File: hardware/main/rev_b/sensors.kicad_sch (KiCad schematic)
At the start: 16 parts, among them U20 ICM-42688-P, U21 LSM6DSO32TR, U22 LPS22DFTR

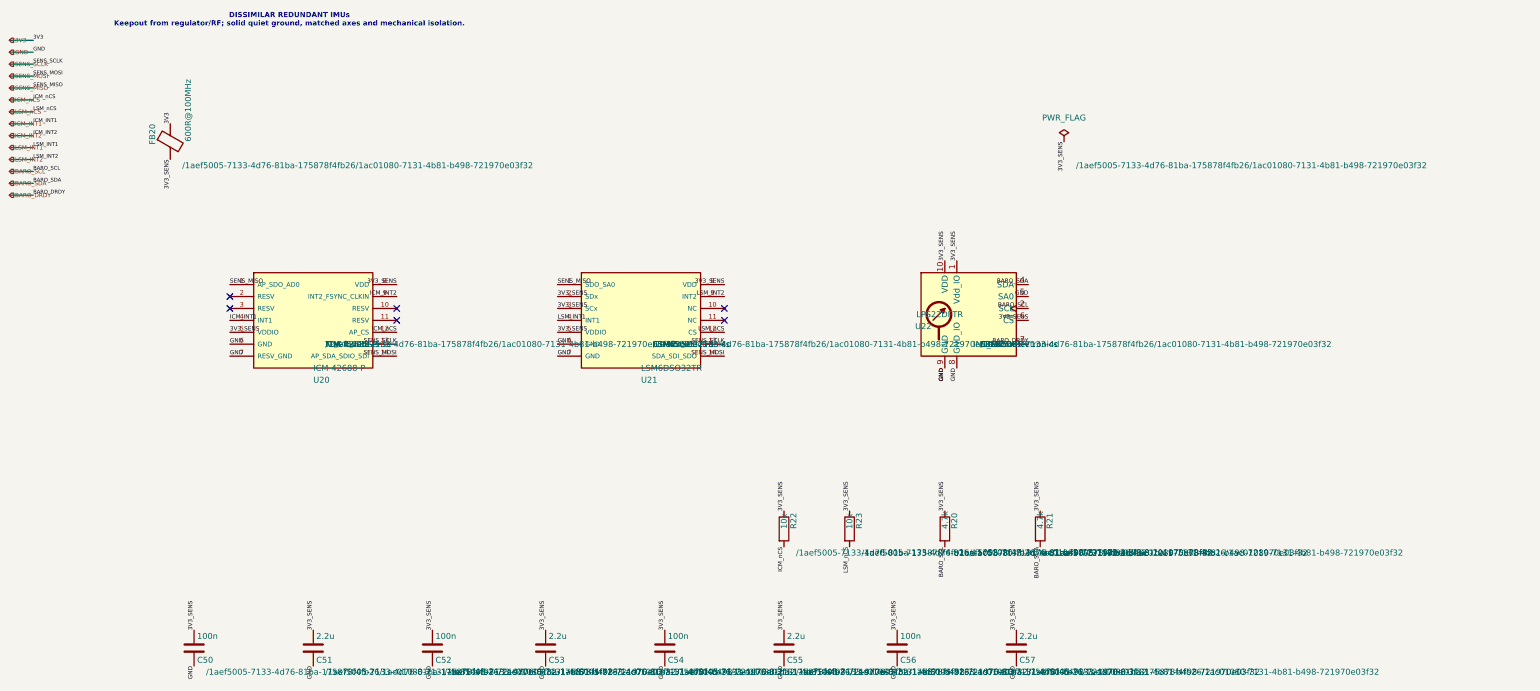
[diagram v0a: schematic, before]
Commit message: build: route and validate rev-b boards
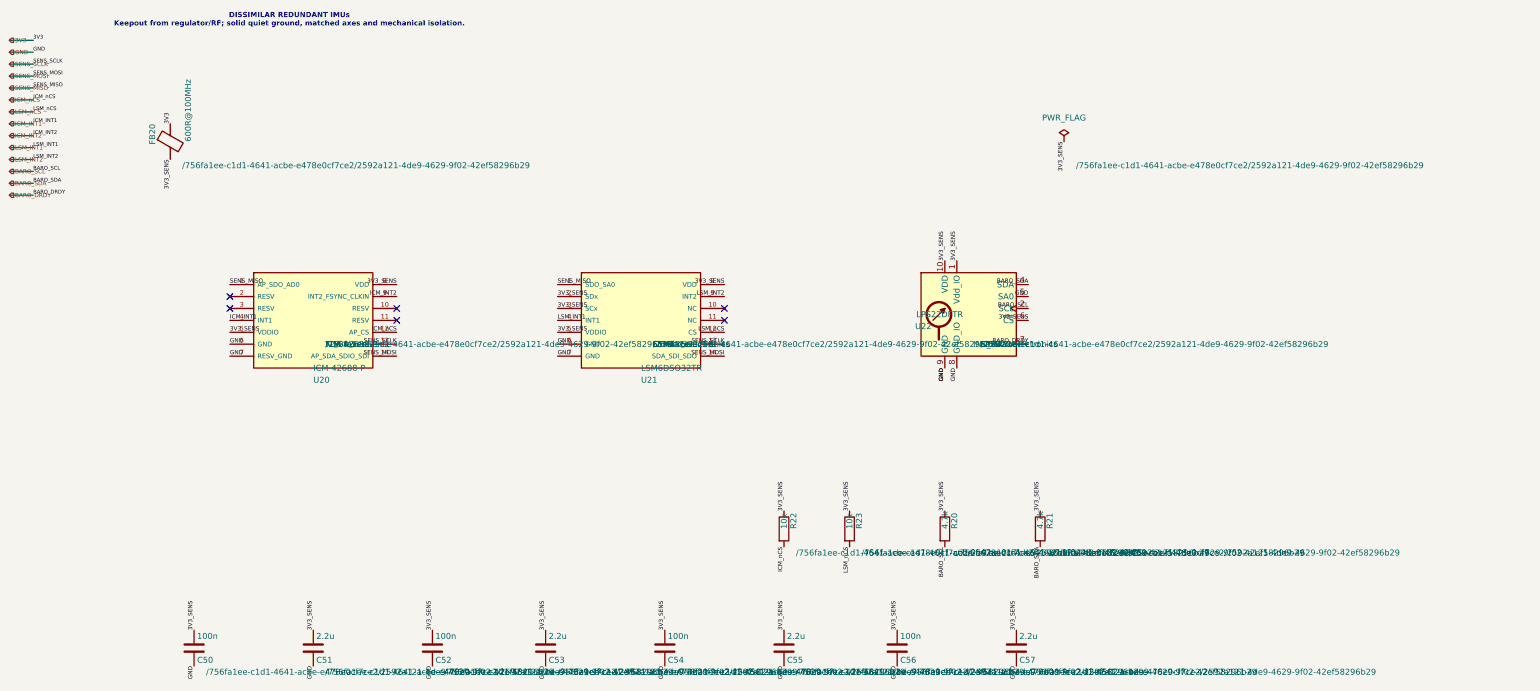
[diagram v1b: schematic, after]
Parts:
- C50, C51, C52, C53, C54, C55, C56, C57, FB20, R20, R21, R22, R23, U20, U21, U22: hierarchy_path /1aef5005-7133-4d76-81ba-175878f4fb26/1ac01080-7131-4b81-b4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 -> /756fa1ee-c1d1-4641-acbe-e478e0cf7ce2/2592a121-4de9-4629-9f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
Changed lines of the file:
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@@
 			)
 		)
-		(property "hierarchy_path" "/1aef5005-7133-4d76-81ba-175878f4fb26/1ac01080-7131-4b81-b498-721970e03f32"
+		(property "hierarchy_path" "/756fa1ee-c1d1-4641-acbe-e478e0cf7ce2/2592a121-4de9-4629-9f02-42ef58296b29"
 			(at 57.15 46.9899 0)
 			(effects
@@
 		(instances
 			(project "main_rev_b"
-				(path "/1aef5005-7133-4d76-81ba-175878f4fb26/1ac01080-7131-4b81-b498-721970e03f32"
+				(path "/756fa1ee-c1d1-4641-acbe-e478e0cf7ce2/2592a121-4de9-4629-9f02-42ef58296b29"
 					(reference "FB20")
 					(unit 1)
@@
 			)
 		)
-		(property "hierarchy_path" "/1aef5005-7133-4d76-81ba-175878f4fb26/1ac01080-7131-4b81-b498-721970e03f32"
+		(property "hierarchy_path" "/756fa1ee-c1d1-4641-acbe-e478e0cf7ce2/2592a121-4de9-4629-9f02-42ef58296b29"
 			(at 87.63 85.0899 0)
 			(effects
@@
 		(instances
 			(project "main_rev_b"
-				(path "/1aef5005-7133-4d76-81ba-175878f4fb26/1ac01080-7131-4b81-b498-721970e03f32"
+				(path "/756fa1ee-c1d1-4641-acbe-e478e0cf7ce2/2592a121-4de9-4629-9f02-42ef58296b29"
 					(reference "U20")
 					(unit 1)
@@
 			)
 		)
-		(property "hierarchy_path" "/1aef5005-7133-4d76-81ba-175878f4fb26/1ac01080-7131-4b81-b498-721970e03f32"
+		(property "hierarchy_path" "/756fa1ee-c1d1-4641-acbe-e478e0cf7ce2/2592a121-4de9-4629-9f02-42ef58296b29"
 			(at 157.48 85.0899 0)
 			(effects
@@
 		(instances
 			(project "main_rev_b"
-				(path "/1aef5005-7133-4d76-81ba-175878f4fb26/1ac01080-7131-4b81-b498-721970e03f32"
+				(path "/756fa1ee-c1d1-4641-acbe-e478e0cf7ce2/2592a121-4de9-4629-9f02-42ef58296b29"
 					(reference "U21")
 					(unit 1)
@@
 			)
 		)
-		(property "hierarchy_path" "/1aef5005-7133-4d76-81ba-175878f4fb26/1ac01080-7131-4b81-b498-721970e03f32"
+		(property "hierarchy_path" "/756fa1ee-c1d1-4641-acbe-e478e0cf7ce2/2592a121-4de9-4629-9f02-42ef58296b29"
 			(at 227.33 85.0899 0)
 			(effects
@@
 		(instances
 			(project "main_rev_b"
-				(path "/1aef5005-7133-4d76-81ba-175878f4fb26/1ac01080-7131-4b81-b498-721970e03f32"
+				(path "/756fa1ee-c1d1-4641-acbe-e478e0cf7ce2/2592a121-4de9-4629-9f02-42ef58296b29"
 					(reference "U22")
 					(unit 1)
@@
 			)
 		)
-		(property "hierarchy_path" "/1aef5005-7133-4d76-81ba-175878f4fb26/1ac01080-7131-4b81-b498-721970e03f32"
+		(property "hierarchy_path" "/756fa1ee-c1d1-4641-acbe-e478e0cf7ce2/2592a121-4de9-4629-9f02-42ef58296b29"
 			(at 222.25 129.5399 0)
 			(effects
@@
 		(instances
 			(project "main_rev_b"
-				(path "/1aef5005-7133-4d76-81ba-175878f4fb26/1ac01080-7131-4b81-b498-721970e03f32"
+				(path "/756fa1ee-c1d1-4641-acbe-e478e0cf7ce2/2592a121-4de9-4629-9f02-42ef58296b29"
 					(reference "R20")
 					(unit 1)
@@
 			)
 		)
-		(property "hierarchy_path" "/1aef5005-7133-4d76-81ba-175878f4fb26/1ac01080-7131-4b81-b498-721970e03f32"
+		(property "hierarchy_path" "/756fa1ee-c1d1-4641-acbe-e478e0cf7ce2/2592a121-4de9-4629-9f02-42ef58296b29"
 			(at 242.57 129.5399 0)
 			(effects
@@
 		(instances
 			(project "main_rev_b"
-				(path "/1aef5005-7133-4d76-81ba-175878f4fb26/1ac01080-7131-4b81-b498-721970e03f32"
+				(path "/756fa1ee-c1d1-4641-acbe-e478e0cf7ce2/2592a121-4de9-4629-9f02-42ef58296b29"
 					(reference "R21")
 					(unit 1)
@@
 			)
 		)
-		(property "hierarchy_path" "/1aef5005-7133-4d76-81ba-175878f4fb26/1ac01080-7131-4b81-b498-721970e03f32"
+		(property "hierarchy_path" "/756fa1ee-c1d1-4641-acbe-e478e0cf7ce2/2592a121-4de9-4629-9f02-42ef58296b29"
 			(at 187.96 129.5399 0)
 			(effects
@@
 		(instances
 			(project "main_rev_b"
-				(path "/1aef5005-7133-4d76-81ba-175878f4fb26/1ac01080-7131-4b81-b498-721970e03f32"
+				(path "/756fa1ee-c1d1-4641-acbe-e478e0cf7ce2/2592a121-4de9-4629-9f02-42ef58296b29"
 					(reference "R22")
 					(unit 1)
@@
 			)
 		)
-		(property "hierarchy_path" "/1aef5005-7133-4d76-81ba-175878f4fb26/1ac01080-7131-4b81-b498-721970e03f32"
+		(property "hierarchy_path" "/756fa1ee-c1d1-4641-acbe-e478e0cf7ce2/2592a121-4de9-4629-9f02-42ef58296b29"
 			(at 201.93 129.5399 0)
 			(effects
@@
 		(instances
 			(project "main_rev_b"
-				(path "/1aef5005-7133-4d76-81ba-175878f4fb26/1ac01080-7131-4b81-b498-721970e03f32"
+				(path "/756fa1ee-c1d1-4641-acbe-e478e0cf7ce2/2592a121-4de9-4629-9f02-42ef58296b29"
 					(reference "R23")
 					(unit 1)
@@
 			)
 		)
-		(property "hierarchy_path" "/1aef5005-7133-4d76-81ba-175878f4fb26/1ac01080-7131-4b81-b498-721970e03f32"
+		(property "hierarchy_path" "/756fa1ee-c1d1-4641-acbe-e478e0cf7ce2/2592a121-4de9-4629-9f02-42ef58296b29"
 			(at 62.23 154.9399 0)
 			(effects
@@
 		(instances
 			(project "main_rev_b"
-				(path "/1aef5005-7133-4d76-81ba-175878f4fb26/1ac01080-7131-4b81-b498-721970e03f32"
+				(path "/756fa1ee-c1d1-4641-acbe-e478e0cf7ce2/2592a121-4de9-4629-9f02-42ef58296b29"
 					(reference "C50")
 					(unit 1)
@@
 			)
 		)
-		(property "hierarchy_path" "/1aef5005-7133-4d76-81ba-175878f4fb26/1ac01080-7131-4b81-b498-721970e03f32"
+		(property "hierarchy_path" "/756fa1ee-c1d1-4641-acbe-e478e0cf7ce2/2592a121-4de9-4629-9f02-42ef58296b29"
 			(at 87.63 154.9399 0)
 			(effects
@@
 		(instances
 			(project "main_rev_b"
-				(path "/1aef5005-7133-4d76-81ba-175878f4fb26/1ac01080-7131-4b81-b498-721970e03f32"
+				(path "/756fa1ee-c1d1-4641-acbe-e478e0cf7ce2/2592a121-4de9-4629-9f02-42ef58296b29"
 					(reference "C51")
 					(unit 1)
@@
 			)
 		)
-		(property "hierarchy_path" "/1aef5005-7133-4d76-81ba-175878f4fb26/1ac01080-7131-4b81-b498-721970e03f32"
+		(property "hierarchy_path" "/756fa1ee-c1d1-4641-acbe-e478e0cf7ce2/2592a121-4de9-4629-9f02-42ef58296b29"
 			(at 113.03 154.9399 0)
 			(effects
@@
 		(instances
 			(project "main_rev_b"
-				(path "/1aef5005-7133-4d76-81ba-175878f4fb26/1ac01080-7131-4b81-b498-721970e03f32"
+				(path "/756fa1ee-c1d1-4641-acbe-e478e0cf7ce2/2592a121-4de9-4629-9f02-42ef58296b29"
 					(reference "C52")
 					(unit 1)
@@
 			)
 		)
-		(property "hierarchy_path" "/1aef5005-7133-4d76-81ba-175878f4fb26/1ac01080-7131-4b81-b498-721970e03f32"
+		(property "hierarchy_path" "/756fa1ee-c1d1-4641-acbe-e478e0cf7ce2/2592a121-4de9-4629-9f02-42ef58296b29"
 			(at 137.16 154.9399 0)
 			(effects
@@
 		(instances
 			(project "main_rev_b"
-				(path "/1aef5005-7133-4d76-81ba-175878f4fb26/1ac01080-7131-4b81-b498-721970e03f32"
+				(path "/756fa1ee-c1d1-4641-acbe-e478e0cf7ce2/2592a121-4de9-4629-9f02-42ef58296b29"
 					(reference "C53")
 					(unit 1)
@@
 			)
 		)
-		(property "hierarchy_path" "/1aef5005-7133-4d76-81ba-175878f4fb26/1ac01080-7131-4b81-b498-721970e03f32"
+		(property "hierarchy_path" "/756fa1ee-c1d1-4641-acbe-e478e0cf7ce2/2592a121-4de9-4629-9f02-42ef58296b29"
 			(at 162.56 154.9399 0)
 			(effects
@@
 		(instances
 			(project "main_rev_b"
-				(path "/1aef5005-7133-4d76-81ba-175878f4fb26/1ac01080-7131-4b81-b498-721970e03f32"
+				(path "/756fa1ee-c1d1-4641-acbe-e478e0cf7ce2/2592a121-4de9-4629-9f02-42ef58296b29"
 					(reference "C54")
 					(unit 1)
@@
 			)
 		)
-		(property "hierarchy_path" "/1aef5005-7133-4d76-81ba-175878f4fb26/1ac01080-7131-4b81-b498-721970e03f32"
+		(property "hierarchy_path" "/756fa1ee-c1d1-4641-acbe-e478e0cf7ce2/2592a121-4de9-4629-9f02-42ef58296b29"
 			(at 187.96 154.9399 0)
 			(effects
@@
 		(instances
 			(project "main_rev_b"
-				(path "/1aef5005-7133-4d76-81ba-175878f4fb26/1ac01080-7131-4b81-b498-721970e03f32"
+				(path "/756fa1ee-c1d1-4641-acbe-e478e0cf7ce2/2592a121-4de9-4629-9f02-42ef58296b29"
 					(reference "C55")
 					(unit 1)
@@
 			)
 		)
-		(property "hierarchy_path" "/1aef5005-7133-4d76-81ba-175878f4fb26/1ac01080-7131-4b81-b498-721970e03f32"
+		(property "hierarchy_path" "/756fa1ee-c1d1-4641-acbe-e478e0cf7ce2/2592a121-4de9-4629-9f02-42ef58296b29"
 			(at 212.09 154.9399 0)
 			(effects
@@
 		(instances
 			(project "main_rev_b"
-				(path "/1aef5005-7133-4d76-81ba-175878f4fb26/1ac01080-7131-4b81-b498-721970e03f32"
+				(path "/756fa1ee-c1d1-4641-acbe-e478e0cf7ce2/2592a121-4de9-4629-9f02-42ef58296b29"
 					(reference "C56")
 					(unit 1)
@@
 			)
 		)
-		(property "hierarchy_path" "/1aef5005-7133-4d76-81ba-175878f4fb26/1ac01080-7131-4b81-b498-721970e03f32"
+		(property "hierarchy_path" "/756fa1ee-c1d1-4641-acbe-e478e0cf7ce2/2592a121-4de9-4629-9f02-42ef58296b29"
 			(at 237.49 154.9399 0)
 			(effects
@@
 		(instances
 			(project "main_rev_b"
-				(path "/1aef5005-7133-4d76-81ba-175878f4fb26/1ac01080-7131-4b81-b498-721970e03f32"
+				(path "/756fa1ee-c1d1-4641-acbe-e478e0cf7ce2/2592a121-4de9-4629-9f02-42ef58296b29"
 					(reference "C57")
 					(unit 1)
@@
 			)
 		)
-		(property "hierarchy_path" "/1aef5005-7133-4d76-81ba-175878f4fb26/1ac01080-7131-4b81-b498-721970e03f32"
+		(property "hierarchy_path" "/756fa1ee-c1d1-4641-acbe-e478e0cf7ce2/2592a121-4de9-4629-9f02-42ef58296b29"
 			(at 247.65 46.9899 0)
 			(effects
@@
 		(instances
 			(project "main_rev_b"
-				(path "/1aef5005-7133-4d76-81ba-175878f4fb26/1ac01080-7131-4b81-b498-721970e03f32"
+				(path "/756fa1ee-c1d1-4641-acbe-e478e0cf7ce2/2592a121-4de9-4629-9f02-42ef58296b29"
 					(reference "#FLG20")
 					(unit 1)
